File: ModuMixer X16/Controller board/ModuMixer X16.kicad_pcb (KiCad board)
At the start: 2 copper layers, 170 x 100 mm, 168 parts, among them J1 Conn_01x03_Pin, J2 Conn_02x04_Counter_Clockwise, J3 Conn_02x07_Counter_Clockwise, J4 Conn_01x05_Pin, J5 Conn_02x07_Counter_Clockwise, J5 Screw_Terminal_01x02, J6 Screw_Terminal_01x02, J6 Screw_Terminal_01x03, J7 Conn_02x03_Counter_Clockwise, J8 Conn_02x25_Counter_Clockwise, J9 Conn_02x25_Counter_Clockwise, Q1 MMBT2222A, Q2 MMBT2222A, Q3 IRF9540N, Q4 MMBT2222A, Q5 MMBT2222A, SW1 Enter, SW10 SW_Push, SW11 SW_Push, SW12 SW_Push, SW13 SW_Push, SW14 SW_Push, SW15 SW_Push, SW16 SW_Push, SW17 SW_Push, SW18 SW_Push, SW19 SW_Push, SW2 Up, SW20 RotaryEncoder_Switch_MP, SW21 RotaryEncoder_Switch_MP, SW22 RotaryEncoder_Switch_MP, SW23 RotaryEncoder_Switch_MP, SW24 RotaryEncoder_Switch_MP, SW25 RotaryEncoder_Switch_MP, SW26 SW_SPST, SW3 Down, SW4 Left, SW5 RotaryEncoder_Switch_MP, SW6 RotaryEncoder_Switch_MP, SW7 RotaryEncoder_Switch_MP, SW8 Right, SW9 SW_Push, U1 STM32F103RCTx, U10 STM32F103RCTx, U11 4016, U12 DRV8833PWP, U2 STM32F103RCTx, U3 LM317_TO-220, U4 LM317_TO-220, U5 LM317_TO-220, U6 LM358, U7 AMS1117-1.8, U8 LM324, U9 TLV320AIC3100, Y1 16MHz, Y2 32.768KHz, Y3 16MHz, Y4 16MHz

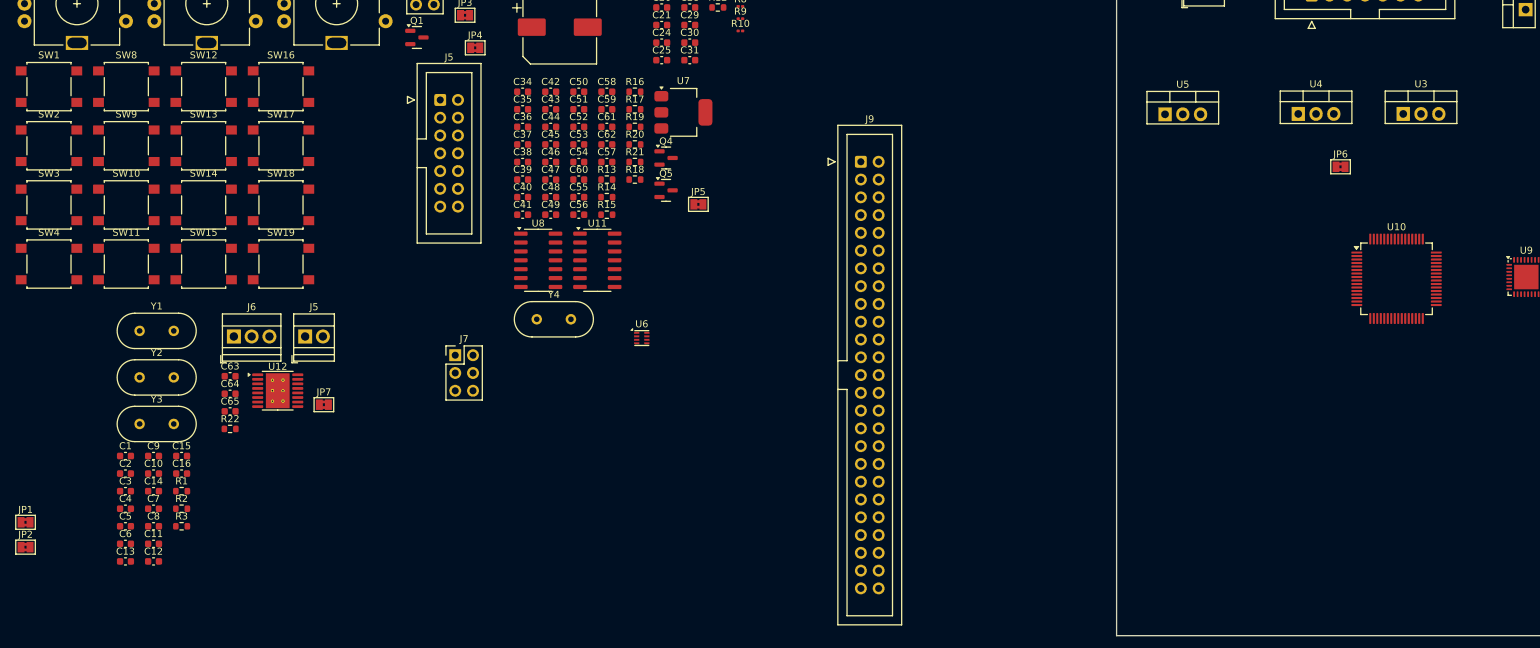
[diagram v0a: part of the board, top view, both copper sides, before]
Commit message: Changed all labels to global
I made it in a rather hacky way (editing all files on notepad with Ctrl + H), i'm only reverting this if something breaks
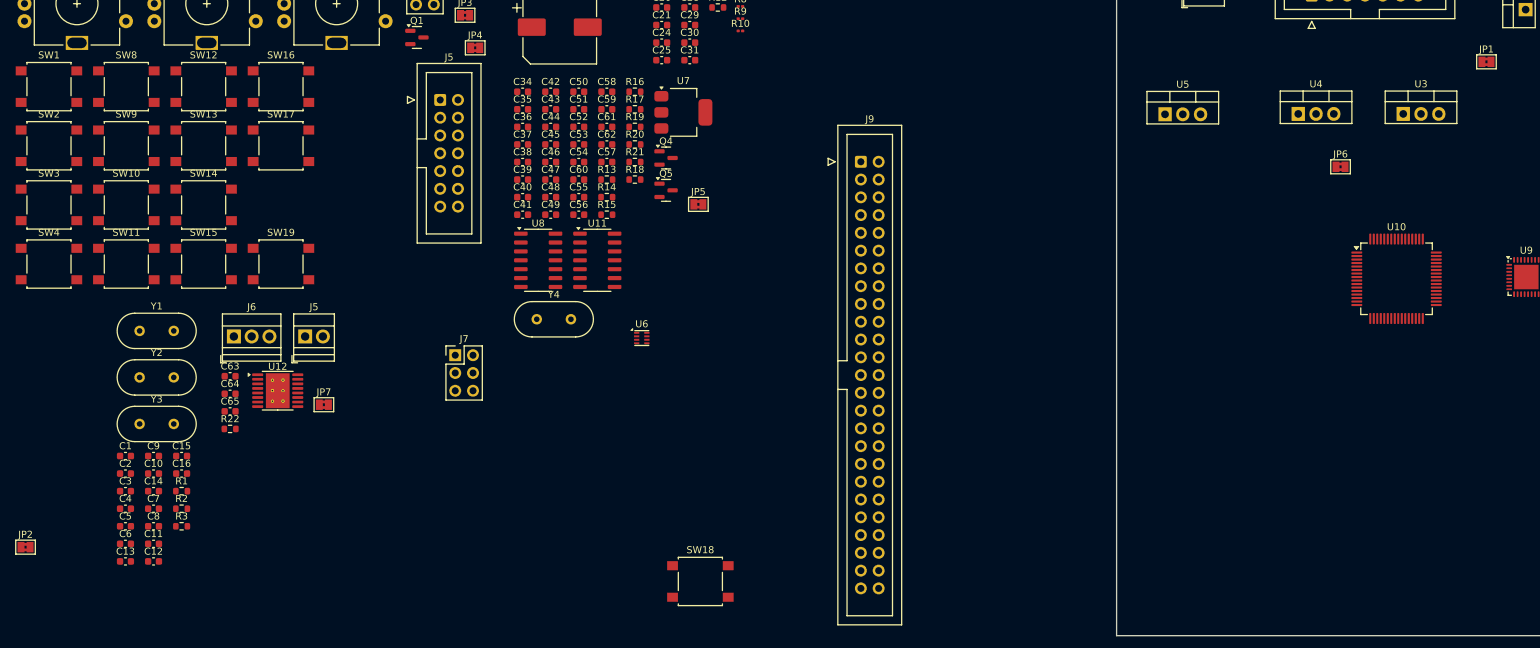
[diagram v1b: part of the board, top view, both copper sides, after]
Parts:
- moved JP1 218.9 mm to (84.8, 54.0)
- moved SW18 80.5 mm to (-27.5, 128.2)
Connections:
- JP1 pad 1: /Core logic/3V3_MAIN -> 3V3_MAIN
- JP2 pad 1: /Core logic/3V3_MAIN -> 3V3_MAIN

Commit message: MCU replacement finished
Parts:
- removed the J5 at (-84.0, 93.2)
- added R23: 1k, Resistor_SMD:R_0603_1608Metric, F.Cu at (-5.83, 92.5)
- added R24: 1k, Resistor_SMD:R_0603_1608Metric, F.Cu at (-5.83, 95.0)
- added R25: 1k, Resistor_SMD:R_0603_1608Metric, F.Cu at (-5.83, 97.5)
- added R26: 1k, Resistor_SMD:R_0603_1608Metric, F.Cu at (-5.83, 100.0)
- added R27: 1k, Resistor_SMD:R_0603_1608Metric, F.Cu at (69.3, 75.5)
- added R28: 1k, Resistor_SMD:R_0603_1608Metric, F.Cu at (69.3, 77.0)
- R10, R5, R6, R7, R8, R9: footprint Resistor_SMD:R_0201_0603Metric -> Resistor_SMD:R_0603_1608Metric
- R3: moved to B.Cu
- moved SW1 448.5 mm to (321.1, 135.5)
- moved SW2 448.5 mm to (321.1, 143.9)
- moved SW3 448.5 mm to (321.1, 152.4)
- moved SW4 448.5 mm to (321.1, 160.8)
- moved SW10 448.5 mm to (332.1, 152.4)
- moved SW11 448.5 mm to (332.1, 160.8)
- moved SW12 448.5 mm to (343.2, 135.5)
- moved SW13 448.5 mm to (343.2, 143.9)
- moved SW14 448.5 mm to (343.2, 152.4)
- moved SW15 448.5 mm to (343.2, 160.8)
- moved SW16 448.5 mm to (354.2, 135.5)
- moved SW17 448.5 mm to (354.2, 143.9)
- moved SW19 448.5 mm to (354.2, 160.8)
- moved SW8 448.5 mm to (332.1, 135.5)
- moved SW9 448.5 mm to (332.1, 143.9)
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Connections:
- net /Core logic/DSP_CLK renamed DSP_CLK
- net /Core logic/DSP_MISO renamed DSP_MISO
- net /Core logic/DSP_MOSI renamed DSP_MOSI
- net /Core logic/DSP_NSS renamed DSP_NSS
- net /Core logic/MAIN_CLK1 renamed MAIN_CLK1
- net /Core logic/MAIN_CLK2 renamed MAIN_CLK2
- net /Core logic/MAIN_RTC1 renamed MAIN_RTC1
- net /Core logic/MAIN_RTC2 renamed MAIN_RTC2
- net /Core logic/MCU_VDD renamed MCU_VDD
- net /Core logic/MOD_READY renamed MOD_READY
- net /Core logic/PERIPHERAL_CLK renamed PERIPHERAL_CLK
- net /Core logic/PERIPHERAL_CLK1 renamed PERIPHERAL_CLK1
- net /Core logic/PERIPHERAL_CLK2 renamed PERIPHERAL_CLK2
- net /Core logic/PERIPHERAL_MISO renamed PERIPHERAL_MISO
- net /Core logic/PERIPHERAL_MOSI renamed PERIPHERAL_MOSI
- net /Core logic/PERIPHERAL_NSS renamed PERIPHERAL_NSS
- net /Core logic/PERIPHERAL_VDD renamed PERIPHERAL_VDD
- net /DSP/1V8_DVDD renamed 1V8_DVDD
- net /DSP/CODEC_NRST renamed CODEC_NRST
- net /DSP/CODEC_SCL renamed CODEC_SCL
- net /DSP/CODEC_SDA renamed CODEC_SDA
- net /DSP/CUE_CTRL renamed CUE_CTRL
- net /DSP/CUE_L renamed CUE_L
- net /DSP/CUE_R renamed CUE_R
- net /DSP/CUE_SEL renamed CUE_SEL
- net /DSP/DSP_3V3 renamed DSP_3V3
- net /DSP/DSP_CLK1 renamed DSP_CLK1
- net /DSP/DSP_CLK2 renamed DSP_CLK2
- net /DSP/DSP_SPI_MISO renamed DSP_SPI_MISO
- net /DSP/DSP_SPI_MOSI renamed DSP_SPI_MOSI
- net /DSP/DSP_SPI_NSS renamed DSP_SPI_NSS
- net /DSP/DSP_SPI_SCK renamed DSP_SPI_SCK
- net /DSP/HPL renamed HPL
- net /DSP/HPR renamed HPR
- net /DSP/HP_L_PRE renamed HP_L_PRE
- net /DSP/HP_R_PRE renamed HP_R_PRE
- net /DSP/I2S_CK renamed I2S_CK
- net /DSP/I2S_EXT_SD renamed I2S_EXT_SD
- net /DSP/I2S_MCK renamed I2S_MCK
- net /DSP/I2S_SD renamed I2S_SD
- net /DSP/I2S_WS renamed I2S_WS
- net /DSP/MAIN_IN_L_M renamed MAIN_IN_L_M
- net /DSP/MAIN_IN_L_P renamed MAIN_IN_L_P
- net /DSP/MAIN_IN_R renamed MAIN_IN_R
- net /DSP/MAIN_IN_R_P renamed MAIN_IN_R_P
- net /DSP/MAIN_L renamed MAIN_L
- net /DSP/MAIN_R renamed MAIN_R
- net /DSP/MAIN_SEL renamed MAIN_SEL
- net /DSP/MIC1LM renamed MIC1LM
- net /DSP/MIC1LP renamed MIC1LP
- net /DSP/MIC1RP renamed MIC1RP
- net /DSP/OUT1_M renamed OUT1_M
- net /DSP/OUT1_P renamed OUT1_P
- net /Fader/FADER_MOTOR_OUT1 renamed FADER_MOTOR_OUT1
- net /Fader/FADER_MOTOR_OUT2 renamed FADER_MOTOR_OUT2
- net /Fader/NSLEEP renamed NSLEEP
- net /Fader/VCP renamed VCP
- net /Fader/VINT renamed VINT
- net /Peripherals/BUZZER_M renamed BUZZER_M
- net /Peripherals/BUZZER_NPN_BASE renamed BUZZER_NPN_BASE
- net /Peripherals/CUE_LM renamed CUE_LM
- net /Peripherals/CUE_LP renamed CUE_LP
- net /Peripherals/CUE_RM renamed CUE_RM
- net /Peripherals/CUE_RP renamed CUE_RP
- net /Peripherals/MAIN_LM renamed MAIN_LM
- net /Peripherals/MAIN_LP renamed MAIN_LP
- net /Peripherals/MAIN_OUT_L_P renamed MAIN_OUT_L_P
- net /Peripherals/MAIN_OUT_R_P renamed MAIN_OUT_R_P
- net /Peripherals/MAIN_RM renamed MAIN_RM
- net /Peripherals/MAIN_RP renamed MAIN_RP
- net /Peripherals/READY renamed READY
- net /Power Supply/+12V_IN renamed 12V_IN
- net /Power Supply/3V3_ALW_FB renamed 3V3_ALW_FB
- net /Power Supply/3V3_MAIN_FB renamed 3V3_MAIN_FB
- net /Power Supply/5V_MAIN_FB renamed 5V_MAIN_FB
- net /Power Supply/MOD_FET_GATE renamed MOD_FET_GATE
- BZ1 pad 1: /Peripherals/5V_MAIN -> 5V_MAIN
- C17 pad 1: /Power Supply/+12V_MAIN -> 12V_MAIN
- C18 pad 1: /Power Supply/+12V_MAIN -> 12V_MAIN
- C19 pad 1: /Power Supply/+12V_MAIN -> 12V_MAIN
- C20 pad 1: /Power Supply/+12V_MAIN -> 12V_MAIN
- C21 pad 1: /Power Supply/+12V_MAIN -> 12V_MAIN
- C22 pad 1: /Power Supply/+12V_MAIN -> 12V_MAIN
- C23 pad 1: /Power Supply/+12V_MAIN -> 12V_MAIN
- C33 pad 1: /Power Supply/+12V_MOD -> 12V_MOD
- C34 pad 2: /DSP/OUT_L_PRE -> OUT_L_PRE
- C35 pad 2: /DSP/OUT_R_PRE -> OUT_R_PRE
- C39 pad 2: /DSP/5V_MAIN -> 5V_MAIN
- C43 pad 1: /DSP/5V_MAIN -> 5V_MAIN
- C44 pad 1: /DSP/5V_MAIN -> 5V_MAIN
- C45 pad 1: /DSP/5V_MAIN -> 5V_MAIN
- C46 pad 1: /DSP/5V_MAIN -> 5V_MAIN
- C60 pad 1: /DSP/5V_MAIN -> 5V_MAIN
- C64 pad 1: /Fader/5V_MAIN -> 5V_MAIN
- C65 pad 1: /Fader/5V_MAIN -> 5V_MAIN
- D1 pad 1: /Power Supply/+12V_MAIN -> 12V_MAIN
- D2 pad 1: /Power Supply/+12V_MAIN -> 12V_MAIN
- J1 pad 1: /Peripherals/HP_L -> HP_L
- J1 pad 2: /Peripherals/HP_R -> HP_R
- J2 pad 2: /Peripherals/5V_MAIN -> 5V_MAIN
- J2 pad 3: /Peripherals/LCD_CS1 -> LCD_CS1
- J2 pad 4: /Peripherals/LCD_CS2 -> LCD_CS2
- J2 pad 5: /Peripherals/LCD_CLK -> LCD_CLK
- J2 pad 6: /Peripherals/LCD_MISO -> LCD_MISO
- J2 pad 7: /Peripherals/LCD_MOSI -> LCD_MOSI
- J3 pad 1: /Peripherals/12V_MOD -> 12V_MOD
- J3 pad 4: /Peripherals/MOD_SCL -> MOD_SCL
- J3 pad 5: /Peripherals/MOD_SDA -> MOD_SDA
- J4 pad 2: /Peripherals/MAIN_OUT_L_M -> MAIN_OUT_L_M
- J4 pad 4: /Peripherals/MAIN_OUT_R_M -> MAIN_OUT_R_M
- J5 pad 1: /Peripherals/MAIN_RESET -> MAIN_RESET
- J5 pad 10: /Peripherals/DSP_BOOT -> DSP_BOOT
- J5 pad 11: /Peripherals/DSP_SWDCLK -> DSP_SWDCLK
- J5 pad 12: /Peripherals/DSP_SWIO -> DSP_SWIO
- J5 pad 13: /Peripherals/3V3_MAIN -> 3V3_MAIN
- J5 pad 2: /Peripherals/MAIN_BOOT -> MAIN_BOOT
- J5 pad 3: /Peripherals/MAIN_SWDCLK -> MAIN_SWDCLK
- J5 pad 4: /Peripherals/MAIN_SWDIO -> MAIN_SWDIO
- J5 pad 5: /Peripherals/PERIPHERAL_RESET -> PERIPHERAL_RESET
- J5 pad 6: /Peripherals/PERIPHERAL_BOOT -> PERIPHERAL_BOOT
- J5 pad 7: /Peripherals/PERIPHERAL_SWDCLK -> PERIPHERAL_SWDCLK
- J5 pad 8: /Peripherals/PERIPHERAL_SWDIO -> PERIPHERAL_SWDIO
- J5 pad 9: /Peripherals/DSP_RESET -> DSP_RESET
- J7 pad 3: /Fader/FADER_W -> FADER_W
- J7 pad 4: /Fader/FADER_A -> FADER_A
- J7 pad 5: /Fader/FADER_B -> FADER_B
- J8 pad 1: /Peripherals/SCRUBBER_A -> SCRUBBER_A
- J8 pad 10: /Peripherals/ENCODER4_B -> ENCODER4_B
- J8 pad 11: /Peripherals/ENCODER5_A -> ENCODER5_A
- J8 pad 12: /Peripherals/ENCODER5_B -> ENCODER5_B
- J8 pad 13: /Peripherals/ENCODER6_A -> ENCODER6_A
- J8 pad 14: /Peripherals/ENCODER6_B -> ENCODER6_B
- J8 pad 15: /Peripherals/ENCODER7_A -> ENCODER7_A
- J8 pad 16: /Peripherals/ENCODER7_B -> ENCODER7_B
- J8 pad 17: /Peripherals/ENCODER8_A -> ENCODER8_A
- J8 pad 18: /Peripherals/ENCODER8_B -> ENCODER8_B
- J8 pad 19: /Peripherals/ENCODER2_SW -> ENCODER2_SW
- J8 pad 2: /Peripherals/SCRUBBER_B -> SCRUBBER_B
- J8 pad 20: /Peripherals/ENCODER1_SW -> ENCODER1_SW
- J8 pad 21: /Peripherals/ENCODER3_SW -> ENCODER3_SW
- J8 pad 22: /Peripherals/ENCODER4_SW -> ENCODER4_SW
- J8 pad 23: /Peripherals/ENCODER5_SW -> ENCODER5_SW
- J8 pad 24: /Peripherals/ENCODER6_SW -> ENCODER6_SW
- J8 pad 25: /Peripherals/ENCODER7_SW -> ENCODER7_SW
- J8 pad 26: /Peripherals/ENCODER8_SW -> ENCODER8_SW
- J8 pad 27: /Peripherals/BTN1 -> BTN1
- J8 pad 28: /Peripherals/BTN2 -> BTN2
- J8 pad 29: /Peripherals/BTN3 -> BTN3
- J8 pad 3: /Peripherals/ENCODER1_A -> ENCODER1_A
- J8 pad 30: /Peripherals/BTN4 -> BTN4
- J8 pad 31: /Peripherals/BTN5 -> BTN5
- J8 pad 32: /Peripherals/BTN6 -> BTN6
- J8 pad 33: /Peripherals/BTN7 -> BTN7
- J8 pad 34: /Peripherals/BTN8 -> BTN8
- J8 pad 35: /Peripherals/BTN9 -> BTN9
- J8 pad 36: /Peripherals/BTN10 -> BTN10
- J8 pad 37: /Peripherals/BTN11 -> BTN11
- J8 pad 38: /Peripherals/BTN12 -> BTN12
- J8 pad 39: /Peripherals/BTN13 -> BTN13
- J8 pad 4: /Peripherals/ENCODER1_B -> ENCODER1_B
- J8 pad 40: /Peripherals/BTN14 -> BTN14
- J8 pad 41: /Peripherals/BTN15 -> BTN15
- J8 pad 42: /Peripherals/BTN16 -> BTN16
- J8 pad 5: /Peripherals/ENCODER2_A -> ENCODER2_A
- J8 pad 6: /Peripherals/ENCODER2_B -> ENCODER2_B
- J8 pad 7: /Peripherals/ENCODER3_A -> ENCODER3_A
- J8 pad 8: /Peripherals/ENCODER3_B -> ENCODER3_B
- J8 pad 9: /Peripherals/ENCODER4_A -> ENCODER4_A
- J9 pad 1: /Peripherals/SCRUBBER_A -> SCRUBBER_A
- J9 pad 10: /Peripherals/ENCODER4_B -> ENCODER4_B
- J9 pad 11: /Peripherals/ENCODER5_A -> ENCODER5_A
- J9 pad 12: /Peripherals/ENCODER5_B -> ENCODER5_B
- J9 pad 13: /Peripherals/ENCODER6_A -> ENCODER6_A
- J9 pad 14: /Peripherals/ENCODER6_B -> ENCODER6_B
- J9 pad 15: /Peripherals/ENCODER7_A -> ENCODER7_A
- J9 pad 16: /Peripherals/ENCODER7_B -> ENCODER7_B
- J9 pad 17: /Peripherals/ENCODER8_A -> ENCODER8_A
- J9 pad 18: /Peripherals/ENCODER8_B -> ENCODER8_B
- J9 pad 19: /Peripherals/ENCODER2_SW -> ENCODER2_SW
- J9 pad 2: /Peripherals/SCRUBBER_B -> SCRUBBER_B
- J9 pad 20: /Peripherals/ENCODER1_SW -> ENCODER1_SW
- J9 pad 21: /Peripherals/ENCODER3_SW -> ENCODER3_SW
- J9 pad 22: /Peripherals/ENCODER4_SW -> ENCODER4_SW
- J9 pad 23: /Peripherals/ENCODER5_SW -> ENCODER5_SW
- J9 pad 24: /Peripherals/ENCODER6_SW -> ENCODER6_SW
- J9 pad 25: /Peripherals/ENCODER7_SW -> ENCODER7_SW
- J9 pad 26: /Peripherals/ENCODER8_SW -> ENCODER8_SW
- J9 pad 27: /Peripherals/BTN1 -> BTN1
- J9 pad 28: /Peripherals/BTN2 -> BTN2
- J9 pad 29: /Peripherals/BTN3 -> BTN3
- J9 pad 3: /Peripherals/ENCODER1_A -> ENCODER1_A
- J9 pad 30: /Peripherals/BTN4 -> BTN4
- J9 pad 31: /Peripherals/BTN5 -> BTN5
- J9 pad 32: /Peripherals/BTN6 -> BTN6
- J9 pad 33: /Peripherals/BTN7 -> BTN7
- J9 pad 34: /Peripherals/BTN8 -> BTN8
- J9 pad 35: /Peripherals/BTN9 -> BTN9
- J9 pad 36: /Peripherals/BTN10 -> BTN10
- J9 pad 37: /Peripherals/BTN11 -> BTN11
- J9 pad 38: /Peripherals/BTN12 -> BTN12
- J9 pad 39: /Peripherals/BTN13 -> BTN13
- J9 pad 4: /Peripherals/ENCODER1_B -> ENCODER1_B
- J9 pad 40: /Peripherals/BTN14 -> BTN14
- J9 pad 41: /Peripherals/BTN15 -> BTN15
- J9 pad 42: /Peripherals/BTN16 -> BTN16
- J9 pad 5: /Peripherals/ENCODER2_A -> ENCODER2_A
- J9 pad 6: /Peripherals/ENCODER2_B -> ENCODER2_B
- J9 pad 7: /Peripherals/ENCODER3_A -> ENCODER3_A
- J9 pad 8: /Peripherals/ENCODER3_B -> ENCODER3_B
- J9 pad 9: /Peripherals/ENCODER4_A -> ENCODER4_A
- JP3 pad 1: /Peripherals/OUT_L_PRE -> OUT_L_PRE
- JP4 pad 2: /Peripherals/OUT_R_PRE -> OUT_R_PRE
- JP5 pad 1: /DSP/3V3_MAIN -> 3V3_MAIN
- JP6 pad 1: /Fader/3V3_MAIN -> 3V3_MAIN
- JP6 pad 2: /Fader/FADER_A -> FADER_A
- JP7 pad 2: /Fader/FADER_B -> FADER_B
- Q3 pad 2: /Power Supply/12V_MAIN -> 12V_MAIN
- Q3 pad 3: /Power Supply/12V_MOD -> 12V_MOD
- Q4 pad 3: /DSP/5V_MAIN -> 5V_MAIN
- R11 pad 1: /Power Supply/MOD_CTRL -> MOD_CTRL
- R12 pad 2: /Power Supply/12V_MAIN -> 12V_MAIN
- R13 pad 1: /DSP/OUT_L_PRE -> OUT_L_PRE
- R14 pad 1: /DSP/OUT_R_PRE -> OUT_R_PRE
- R15 pad 2: /DSP/MAIN_OUT_L_M -> MAIN_OUT_L_M
- R16 pad 2: /DSP/MAIN_OUT_R_M -> MAIN_OUT_R_M
- R21 pad 2: /DSP/5V_MAIN -> 5V_MAIN
- R22 pad 1: /Fader/5V_MAIN -> 5V_MAIN
- R4 pad 1: /Peripherals/BUZZER_CTRL -> BUZZER_CTRL
- SW1 pad 2: /Peripherals/BTN1 -> BTN1
- SW10 pad 2: /Peripherals/BTN7 -> BTN7
- SW11 pad 2: /Peripherals/BTN8 -> BTN8
- SW12 pad 2: /Peripherals/BTN9 -> BTN9
- SW13 pad 2: /Peripherals/BTN10 -> BTN10
- SW14 pad 2: /Peripherals/BTN11 -> BTN11
- SW15 pad 2: /Peripherals/BTN12 -> BTN12
- SW16 pad 2: /Peripherals/BTN13 -> BTN13
- SW17 pad 2: /Peripherals/BTN14 -> BTN14
- SW18 pad 2: /Peripherals/BTN15 -> BTN15
- SW19 pad 2: /Peripherals/BTN16 -> BTN16
- SW2 pad 2: /Peripherals/BTN2 -> BTN2
- SW20 pad A: /Peripherals/ENCODER3_A -> ENCODER3_A
- SW20 pad B: /Peripherals/ENCODER3_B -> ENCODER3_B
- SW20 pad S1: /Peripherals/ENCODER3_SW -> ENCODER3_SW
- SW21 pad A: /Peripherals/ENCODER4_A -> ENCODER4_A
- SW21 pad B: /Peripherals/ENCODER4_B -> ENCODER4_B
- SW21 pad S1: /Peripherals/ENCODER4_SW -> ENCODER4_SW
- SW22 pad A: /Peripherals/ENCODER5_A -> ENCODER5_A
- SW22 pad B: /Peripherals/ENCODER5_B -> ENCODER5_B
- SW22 pad S1: /Peripherals/ENCODER5_SW -> ENCODER5_SW
- SW23 pad A: /Peripherals/ENCODER6_A -> ENCODER6_A
- SW23 pad B: /Peripherals/ENCODER6_B -> ENCODER6_B
- SW23 pad S1: /Peripherals/ENCODER6_SW -> ENCODER6_SW
- SW24 pad A: /Peripherals/ENCODER7_A -> ENCODER7_A
- SW24 pad B: /Peripherals/ENCODER7_B -> ENCODER7_B
- SW24 pad S1: /Peripherals/ENCODER7_SW -> ENCODER7_SW
- SW25 pad A: /Peripherals/ENCODER8_A -> ENCODER8_A
- SW25 pad B: /Peripherals/ENCODER8_B -> ENCODER8_B
- SW25 pad S1: /Peripherals/ENCODER8_SW -> ENCODER8_SW
- SW26 pad 2: /Power Supply/+12V_MAIN -> 12V_MAIN
- SW3 pad 2: /Peripherals/BTN3 -> BTN3
- SW4 pad 2: /Peripherals/BTN4 -> BTN4
- SW5 pad A: /Peripherals/ENCODER1_A -> ENCODER1_A
- SW5 pad B: /Peripherals/ENCODER1_B -> ENCODER1_B
- SW5 pad S1: /Peripherals/ENCODER1_SW -> ENCODER1_SW
- SW6 pad A: /Peripherals/ENCODER2_A -> ENCODER2_A
- SW6 pad B: /Peripherals/ENCODER2_B -> ENCODER2_B
- SW6 pad S1: /Peripherals/ENCODER2_SW -> ENCODER2_SW
- SW7 pad A: /Peripherals/SCRUBBER_A -> SCRUBBER_A
- SW7 pad B: /Peripherals/SCRUBBER_B -> SCRUBBER_B
- SW8 pad 2: /Peripherals/BTN5 -> BTN5
- SW9 pad 2: /Peripherals/BTN6 -> BTN6
- U1 pad 1: /Core logic/3V3_STBY -> 3V3_STBY
- U1 pad 14: /Core logic/BUZZER_CTRL -> BUZZER_CTRL
- U1 pad 27: /Core logic/FADER_MOTOR_IN2 -> FADER_MOTOR_IN2
- U1 pad 28: /Core logic/FADER_MOTOR_IN1 -> FADER_MOTOR_IN1
- U1 pad 29: /Core logic/MOD_SCL -> MOD_SCL
- U1 pad 30: /Core logic/MOD_SDA -> MOD_SDA
- U1 pad 45: /Core logic/LCD_CS1 -> LCD_CS1
- U1 pad 46: /Core logic/MAIN_SWDIO -> MAIN_SWDIO
- U1 pad 49: /Core logic/MAIN_SWDCLK -> MAIN_SWDCLK
- U1 pad 50: /Core logic/LCD_CS2 -> LCD_CS2
- U1 pad 55: /Core logic/LCD_CLK -> LCD_CLK
- U1 pad 56: /Core logic/LCD_MISO -> LCD_MISO
- U1 pad 57: /Core logic/LCD_MOSI -> LCD_MOSI
- U1 pad 58: /Core logic/FADER_W -> FADER_W
- U1 pad 59: /Core logic/MOD_CTRL -> MOD_CTRL
- U1 pad 60: /Core logic/MAIN_BOOT -> MAIN_BOOT
- U1 pad 7: /Core logic/MAIN_RESET -> MAIN_RESET
- U10 pad 46: /DSP/DSP_SWIO -> DSP_SWIO
- U10 pad 49: /DSP/DSP_SWDCLK -> DSP_SWDCLK
- U10 pad 60: /DSP/DSP_BOOT -> DSP_BOOT
- U10 pad 7: /DSP/DSP_RESET -> DSP_RESET
- U11 pad 14: /DSP/5V_MAIN -> 5V_MAIN
- U12 pad 10: /Fader/FADER_MOTOR_IN2 -> FADER_MOTOR_IN2
- U12 pad 12: /Fader/5V_MAIN -> 5V_MAIN
- U12 pad 15: /Fader/FADER_MOTOR_IN2 -> FADER_MOTOR_IN2
- U12 pad 16: /Fader/FADER_MOTOR_IN1 -> FADER_MOTOR_IN1
- U12 pad 9: /Fader/FADER_MOTOR_IN1 -> FADER_MOTOR_IN1
- U2 pad 1: /Core logic/3V3_STBY -> 3V3_STBY
- U2 pad 10: /Core logic/BTN3 -> BTN3
- U2 pad 11: /Core logic/BTN4 -> BTN4
- U2 pad 14: /Core logic/SCRUBBER_A -> SCRUBBER_A
- U2 pad 15: /Core logic/SCRUBBER_B -> SCRUBBER_B
- U2 pad 16: /Core logic/ENCODER1_A -> ENCODER1_A
- U2 pad 17: /Core logic/ENCODER1_B -> ENCODER1_B
- U2 pad 2: /Core logic/BTN14 -> BTN14
- U2 pad 24: /Core logic/BTN5 -> BTN5
- U2 pad 25: /Core logic/BTN6 -> BTN6
- U2 pad 26: /Core logic/ENCODER5_A -> ENCODER5_A
- U2 pad 27: /Core logic/ENCODER5_B -> ENCODER5_B
- U2 pad 28: /Core logic/ENCODER6_A -> ENCODER6_A
- U2 pad 29: /Core logic/ENCODER3_SW -> ENCODER3_SW
- U2 pad 3: /Core logic/BTN15 -> BTN15
- U2 pad 30: /Core logic/ENCODER4_SW -> ENCODER4_SW
- U2 pad 33: /Core logic/ENCODER5_SW -> ENCODER5_SW
- U2 pad 34: /Core logic/ENCODER6_SW -> ENCODER6_SW
- U2 pad 35: /Core logic/ENCODER7_SW -> ENCODER7_SW
- U2 pad 36: /Core logic/ENCODER8_SW -> ENCODER8_SW
- U2 pad 37: /Core logic/BTN7 -> BTN7
- U2 pad 38: /Core logic/BTN8 -> BTN8
- U2 pad 39: /Core logic/BTN9 -> BTN9
- U2 pad 4: /Core logic/BTN16 -> BTN16
- U2 pad 40: /Core logic/BTN10 -> BTN10
- U2 pad 41: /Core logic/ENCODER2_A -> ENCODER2_A
- U2 pad 42: /Core logic/ENCODER2_B -> ENCODER2_B
- U2 pad 43: /Core logic/ENCODER3_A -> ENCODER3_A
- U2 pad 44: /Core logic/ENCODER3_B -> ENCODER3_B
- U2 pad 45: /Core logic/ENCODER4_A -> ENCODER4_A
- U2 pad 46: /Core logic/PERIPHERAL_SWDIO -> PERIPHERAL_SWDIO
- U2 pad 49: /Core logic/PERIPHERAL_SWDCLK -> PERIPHERAL_SWDCLK
- U2 pad 50: /Core logic/ENCODER4_B -> ENCODER4_B
- U2 pad 51: /Core logic/BTN11 -> BTN11
- U2 pad 52: /Core logic/BTN12 -> BTN12
- U2 pad 53: /Core logic/BTN13 -> BTN13
- U2 pad 55: /Core logic/ENCODER6_B -> ENCODER6_B
- U2 pad 56: /Core logic/ENCODER7_A -> ENCODER7_A
- U2 pad 57: /Core logic/ENCODER7_B -> ENCODER7_B
- U2 pad 58: /Core logic/ENCODER8_A -> ENCODER8_A
- U2 pad 59: /Core logic/ENCODER8_B -> ENCODER8_B
- U2 pad 60: /Core logic/PERIPHERAL_BOOT -> PERIPHERAL_BOOT
- U2 pad 61: /Core logic/ENCODER1_SW -> ENCODER1_SW
- U2 pad 62: /Core logic/ENCODER2_SW -> ENCODER2_SW
- U2 pad 7: /Core logic/PERIPHERAL_RESET -> PERIPHERAL_RESET
- U2 pad 8: /Core logic/BTN1 -> BTN1
- U2 pad 9: /Core logic/BTN2 -> BTN2
- U3 pad 3: /Power Supply/+12V_MAIN -> 12V_MAIN
- U4 pad 3: /Power Supply/+12V_MAIN -> 12V_MAIN
- U8 pad 1: /DSP/MAIN_OUT_R_M -> MAIN_OUT_R_M
- U8 pad 14: /DSP/MAIN_OUT_L_M -> MAIN_OUT_L_M
- U8 pad 4: /DSP/5V_MAIN -> 5V_MAIN
- U8 pad 6: /DSP/HP_R -> HP_R
- U8 pad 7: /DSP/HP_R -> HP_R
- U8 pad 8: /DSP/HP_L -> HP_L
- U8 pad 9: /DSP/HP_L -> HP_L
- U9 pad 21: /DSP/5V_MAIN -> 5V_MAIN
- U9 pad 24: /DSP/5V_MAIN -> 5V_MAIN
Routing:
- net FADER_W: track 0.00 -> 216.6 mm, vias 0 -> 1
- net 5V_MAIN: track 0.00 -> 119.6 mm
- net 12V_MAIN: track 0.00 -> 104.0 mm
- net 12V_MOD: track 0.00 -> 36.0 mm
- net 12V_IN: track 0.00 -> 32.0 mm
- net FADER_MOTOR_OUT2: track 0.00 -> 24.8 mm, vias 0 -> 1
- net FADER_MOTOR_OUT1: track 0.00 -> 23.3 mm, vias 0 -> 2
- net MAIN_RTC2: track 0.00 -> 17.3 mm
- net MAIN_RTC1: track 0.00 -> 14.7 mm
- net FADER_B: track 0.00 -> 14.4 mm
- net FADER_MOTOR_IN2: track 0.00 -> 14.4 mm, vias 0 -> 2
- net PERIPHERAL_CLK2: track 0.00 -> 13.2 mm
- net FADER_MOTOR_IN1: track 0.00 -> 12.8 mm, vias 0 -> 2
- net 5V_MAIN_FB: track 0.00 -> 12.0 mm
- net PERIPHERAL_CLK1: track 0.00 -> 11.2 mm
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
